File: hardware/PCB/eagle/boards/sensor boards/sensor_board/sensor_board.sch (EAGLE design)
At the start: 22 parts

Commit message: updated boards with new components
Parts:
- GND, PWR, PWR_EXT, PWR_INT: device SparkFun-Connectors:M02PTH -> passive_components:M02PTH
- JP1, JP2: device SparkFun-Connectors:M04PTH -> passive_components:M04PTH
- MCU2: device SparkFun-Connectors:M09 -> passive_components:M09
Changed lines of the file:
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@@
 <grid distance="0.1" unitdist="inch" unit="inch" style="lines" multiple="1" display="no" altdistance="0.01" altunitdist="inch" altunit="inch"/>
 <layers>
-<layer number="1" name="Top" color="4" fill="1" visible="no" active="no"/>
-<layer number="16" name="Bottom" color="1" fill="1" visible="no" active="no"/>
-<layer number="17" name="Pads" color="2" fill="1" visible="no" active="no"/>
-<layer number="18" name="Vias" color="2" fill="1" visible="no" active="no"/>
-<layer number="19" name="Unrouted" color="6" fill="1" visible="no" active="no"/>
-<layer number="20" name="Dimension" color="15" fill="1" visible="no" active="no"/>
-<layer number="21" name="tPlace" color="7" fill="1" visible="no" active="no"/>
-<layer number="22" name="bPlace" color="7" fill="1" visible="no" active="no"/>
-<layer number="23" name="tOrigins" color="15" fill="1" visible="no" active="no"/>
-<layer number="24" name="bOrigins" color="15" fill="1" visible="no" active="no"/>
-<layer number="25" name="tNames" color="7" fill="1" visible="no" active="no"/>
-<layer number="26" name="bNames" color="7" fill="1" visible="no" active="no"/>
-<layer number="27" name="tValues" color="7" fill="1" visible="no" active="no"/>
-<layer number="28" name="bValues" color="7" fill="1" visible="no" active="no"/>
+<layer number="1" name="Top" color="4" fill="1" visible="yes" active="no"/>
+<layer number="16" name="Bottom" color="1" fill="1" visible="yes" active="no"/>
+<layer number="17" name="Pads" color="2" fill="1" visible="yes" active="no"/>
+<layer number="18" name="Vias" color="2" fill="1" visible="yes" active="no"/>
+<layer number="19" name="Unrouted" color="6" fill="1" visible="yes" active="no"/>
+<layer number="20" name="Dimension" color="15" fill="1" visible="yes" active="no"/>
+<layer number="21" name="tPlace" color="7" fill="1" visible="yes" active="no"/>
+<layer number="22" name="bPlace" color="7" fill="1" visible="yes" active="no"/>
+<layer number="23" name="tOrigins" color="15" fill="1" visible="yes" active="no"/>
+<layer number="24" name="bOrigins" color="15" fill="1" visible="yes" active="no"/>
+<layer number="25" name="tNames" color="7" fill="1" visible="yes" active="no"/>
+<layer number="26" name="bNames" color="7" fill="1" visible="yes" active="no"/>
+<layer number="27" name="tValues" color="7" fill="1" visible="yes" active="no"/>
+<layer number="28" name="bValues" color="7" fill="1" visible="yes" active="no"/>
 <layer number="29" name="tStop" color="7" fill="3" visible="no" active="no"/>
 <layer number="30" name="bStop" color="7" fill="6" visible="no" active="no"/>
@@
 <layer number="35" name="tGlue" color="7" fill="4" visible="no" active="no"/>
 <layer number="36" name="bGlue" color="7" fill="5" visible="no" active="no"/>
-<layer number="37" name="tTest" color="7" fill="1" visible="no" active="no"/>
-<layer number="38" name="bTest" color="7" fill="1" visible="no" active="no"/>
+<layer number="37" name="tTest" color="7" fill="1" visible="yes" active="no"/>
+<layer number="38" name="bTest" color="7" fill="1" visible="yes" active="no"/>
 <layer number="39" name="tKeepout" color="4" fill="11" visible="no" active="no"/>
 <layer number="40" name="bKeepout" color="1" fill="11" visible="no" active="no"/>
@@
 <layer number="44" name="Drills" color="7" fill="1" visible="no" active="no"/>
 <layer number="45" name="Holes" color="7" fill="1" visible="no" active="no"/>
-<layer number="46" name="Milling" color="3" fill="1" visible="no" active="no"/>
-<layer number="47" name="Measures" color="7" fill="1" visible="no" active="no"/>
-<layer number="48" name="Document" color="7" fill="1" visible="no" active="no"/>
-<layer number="49" name="Reference" color="7" fill="1" visible="no" active="no"/>
-<layer number="50" name="dxf" color="7" fill="1" visible="no" active="no"/>
-<layer number="51" name="tDocu" color="7" fill="1" visible="no" active="no"/>
-<layer number="52" name="bDocu" color="7" fill="1" visible="no" active="no"/>
-<layer number="53" name="tGND_GNDA" color="7" fill="9" visible="no" active="no"/>
-<layer number="54" name="bGND_GNDA" color="1" fill="9" visible="no" active="no"/>
-<layer number="56" name="wert" color="7" fill="1" visible="no" active="no"/>
-<layer number="57" name="tCAD" color="7" fill="1" visible="no" active="no"/>
+<layer number="46" name="Milling" color="3" fill="1" visible="yes" active="no"/>
+<layer number="47" name="Measures" color="7" fill="1" visible="yes" active="no"/>
+<layer number="48" name="Document" color="7" fill="1" visible="yes" active="no"/>
+<layer number="49" name="Reference" color="7" fill="1" visible="yes" active="no"/>
+<layer number="50" name="dxf" color="7" fill="1" visible="yes" active="no"/>
+<layer number="51" name="tDocu" color="7" fill="1" visible="yes" active="no"/>
+<layer number="52" name="bDocu" color="7" fill="1" visible="yes" active="no"/>
+<layer number="53" name="tGND_GNDA" color="7" fill="9" visible="yes" active="no"/>
+<layer number="54" name="bGND_GNDA" color="1" fill="9" visible="yes" active="no"/>
+<layer number="56" name="wert" color="7" fill="1" visible="yes" active="no"/>
+<layer number="57" name="tCAD" color="7" fill="1" visible="yes" active="no"/>
 <layer number="90" name="Modules" color="5" fill="1" visible="yes" active="yes"/>
 <layer number="91" name="Nets" color="2" fill="1" visible="yes" active="yes"/>
@@
 <part name="R1" library="SparkFun-Resistors" deviceset="10KOHM-1/4W5%(PTH)" device="" value="10k"/>
 <part name="R2" library="SparkFun-Resistors" deviceset="10KOHM-1/4W5%(PTH)" device="" value="10k"/>
-<part name="MCU2" library="SparkFun-Connectors" deviceset="M09" device=""/>
+<part name="MCU2" library="passive_components" deviceset="M09" device=""/>
 <part name="SHT1" library="pinhead" deviceset="PINHD-1X4" device=""/>
 <part name="SHT2" library="pinhead" deviceset="PINHD-1X4" device=""/>
@@
 <part name="VBT1" library="pinhead" deviceset="PINHD-1X4" device=""/>
 <part name="VBT2" library="pinhead" deviceset="PINHD-1X4" device=""/>
-<part name="JP1" library="SparkFun-Connectors" deviceset="M04" device="PTH"/>
-<part name="JP2" library="SparkFun-Connectors" deviceset="M04" device="PTH"/>
-<part name="GND" library="SparkFun-Connectors" deviceset="M02" device="PTH"/>
-<part name="PWR" library="SparkFun-Connectors" deviceset="M02" device="PTH"/>
-<part name="PWR_EXT" library="SparkFun-Connectors" deviceset="M02" device="PTH"/>
-<part name="PWR_INT" library="SparkFun-Connectors" deviceset="M02" device="PTH"/>
+<part name="JP1" library="passive_components" deviceset="M04" device="PTH"/>
+<part name="JP2" library="passive_components" deviceset="M04" device="PTH"/>
+<part name="GND" library="passive_components" deviceset="M02" device="PTH"/>
+<part name="PWR" library="passive_components" deviceset="M02" device="PTH"/>
+<part name="PWR_EXT" library="passive_components" deviceset="M02" device="PTH"/>
+<part name="PWR_INT" library="passive_components" deviceset="M02" device="PTH"/>
 </parts>
 <sheets>

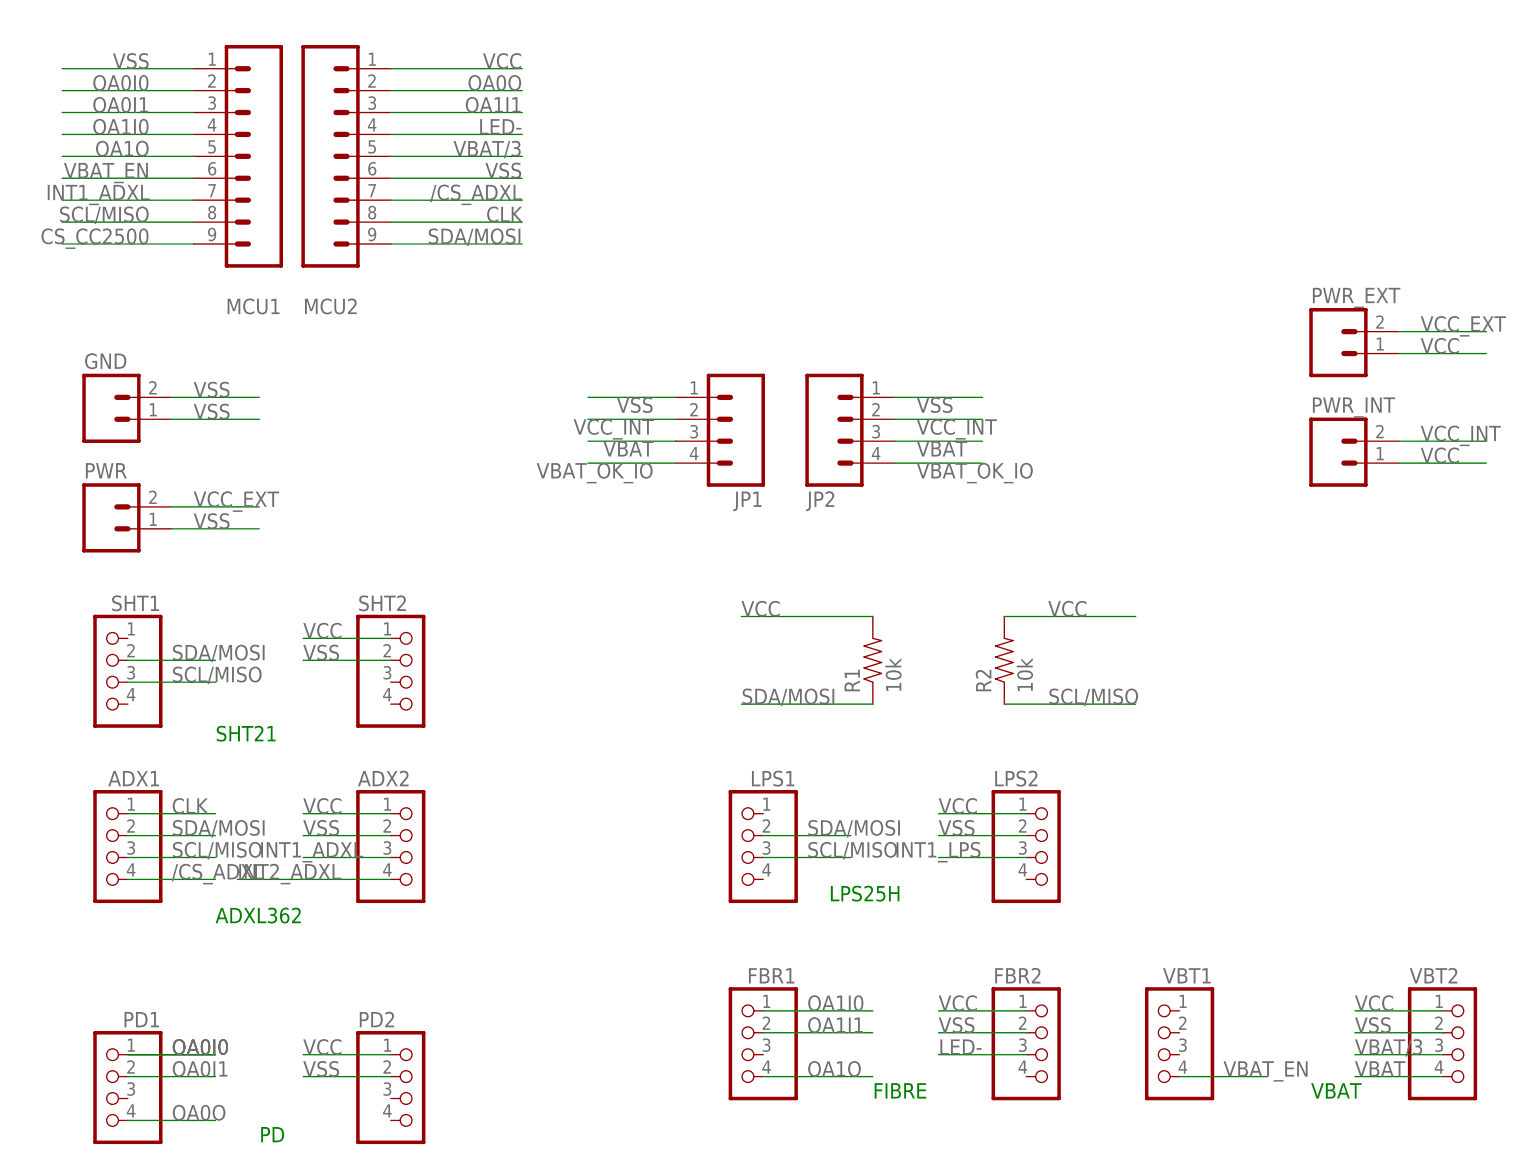
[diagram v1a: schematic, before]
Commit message: adjusted spacing on sensor board
- increased the spacing between components on the sensor board to aid
visibility of the values and names on the board
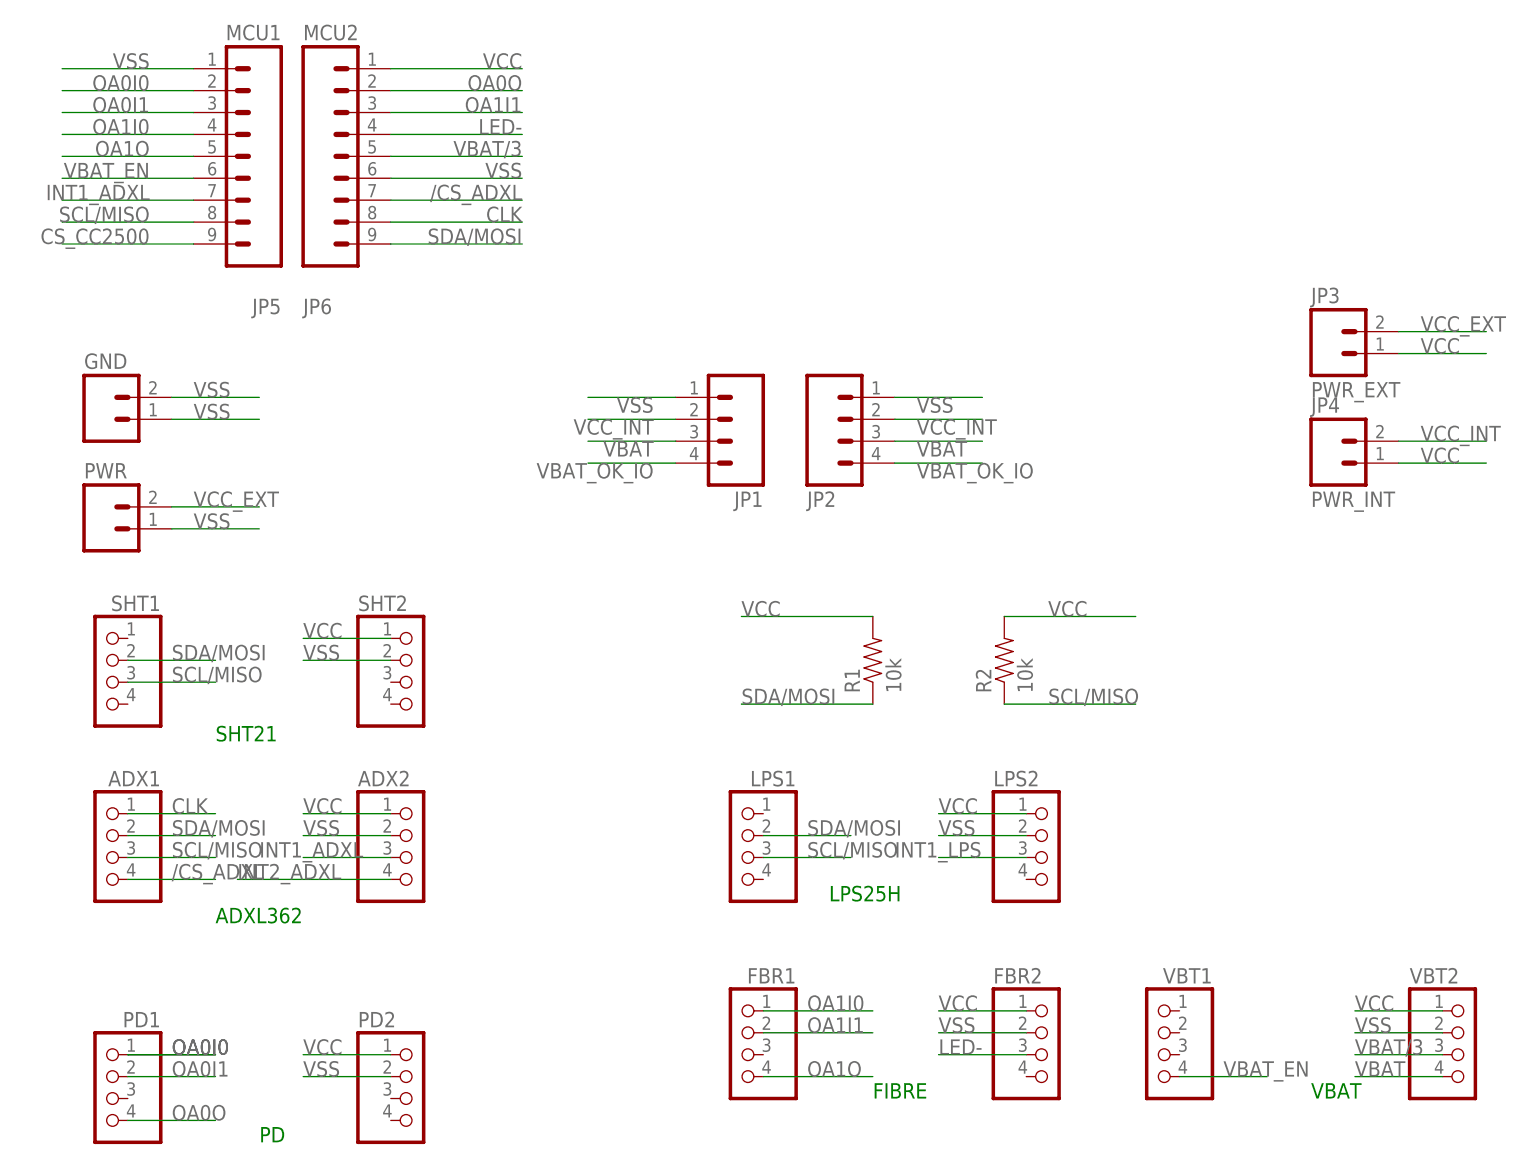
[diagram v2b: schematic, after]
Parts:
- JP3: value (none) -> PWR_EXT
- JP4: value (none) -> PWR_INT
- JP5: value (none) -> MCU1
- JP6: value (none) -> MCU2
- renumbered MCU1 to JP5, MCU2 to JP6, PWR_EXT to JP3, PWR_INT to JP4
